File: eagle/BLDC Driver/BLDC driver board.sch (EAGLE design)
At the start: 25 parts, among them J1 SCREWTERM02, Q1 MOSFET-NCHANNEL, Q2 MOSFET-NCHANNEL, Q3 MOSFET-NCHANNEL, Q4 MOSFET-NCHANNEL, Q5 MOSFET-NCHANNEL, Q6 MOSFET-NCHANNEL, U2 AUIRS2334S

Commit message: Started working on new driver board.
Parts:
- removed D1, D2, D6: (no value), CMPE118lib:DIODEHV
- removed U2: AUIRS2334S, ASL:AUIRS2334S
- added 5V: (no value), jumper:JP1E
- added C5, C6: (no value), ASL:CAP0805
- added R2: (no value), ASL:RESISTOR0805-RES
- added U$2: DRV8302, ASL:DRV8302
- C1: value 470nF -> .1uF; device CMPE118lib:CAP1206 -> ASL:CAP0805
- C2: value 470nF -> 4.7uF; device CMPE118lib:CAP1206 -> ASL:CAP0805
- C3: value 470nF -> .015uF; device CMPE118lib:CAP1206 -> ASL:CAP0805
- C4: value 1uF -> (none); device CMPE118lib:CAP1206 -> ASL:CAP0805
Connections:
- removed net N$11: C3.1, D6.C, U2.VB3
- new net CRRNTSNS1: U$1.RA2
- new net CRRNTSNS2: U$1.RA0
- new net N$1: C3.2, U$2.SS_TR
- new net N$4: C4.1, U$2.BST_A
- new net N$5: C4.2, U$2.SH_A
- new net N$6: C5.1, U$2.BST_B
- new net N$8: C6.1, U$2.BST_C
- new net N$9: C6.2, U$2.SH_C
- new net PGND: Q2.S, Q4.S, Q6.S, U$2.GND
- new net PVDD: C1.1, C2.1, Q1.D, Q3.D, Q5.D, U$2.PVDD1, U$2.PVDD2, U$2.PVDD2(1)
- net +UB: no longer Q1.D, Q3.D, Q5.D
- net -UB: no longer Q2.S, Q4.S, Q6.S
- net GND: now also 5V.1, C1.2, C2.2, C3.1, R2.2; no longer C4.2, U2.COM
- net HO1: no longer U2.HO1
- net HO2: no longer U2.HO2
- net HO3: no longer U2.HO3
- net LO1: no longer U2.LO1
- net LO2: no longer U2.LO2
- net LO3: no longer U2.LO3
- net N$3: now also R2.1, U$2.BIAS; no longer C1.1, D1.C, U2.VB1
- net N$7: now also C5.2, U$2.SH_B; no longer C2.1, D2.C, U2.VB2
- net OUTPUTA: no longer C1.2, U2.VS1
- net OUTPUTB: no longer C2.2, U2.VS2
- net OUTPUTC: no longer C3.2, U2.VS3
- net PWM1: now also U$2.INH_A; no longer U2.HIN1, U2.LIN1
- net PWM2: now also U$2.INH_B; no longer U2.HIN2, U2.LIN2
- net PWM3: now also U$2.INH_C; no longer U2.HIN3, U2.LIN3
- net VCC: now also 5V.2; no longer C4.1, D1.A, D2.A, D6.A, U2.VCC
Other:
- moved on the sheet: C1, C2, C3, C4

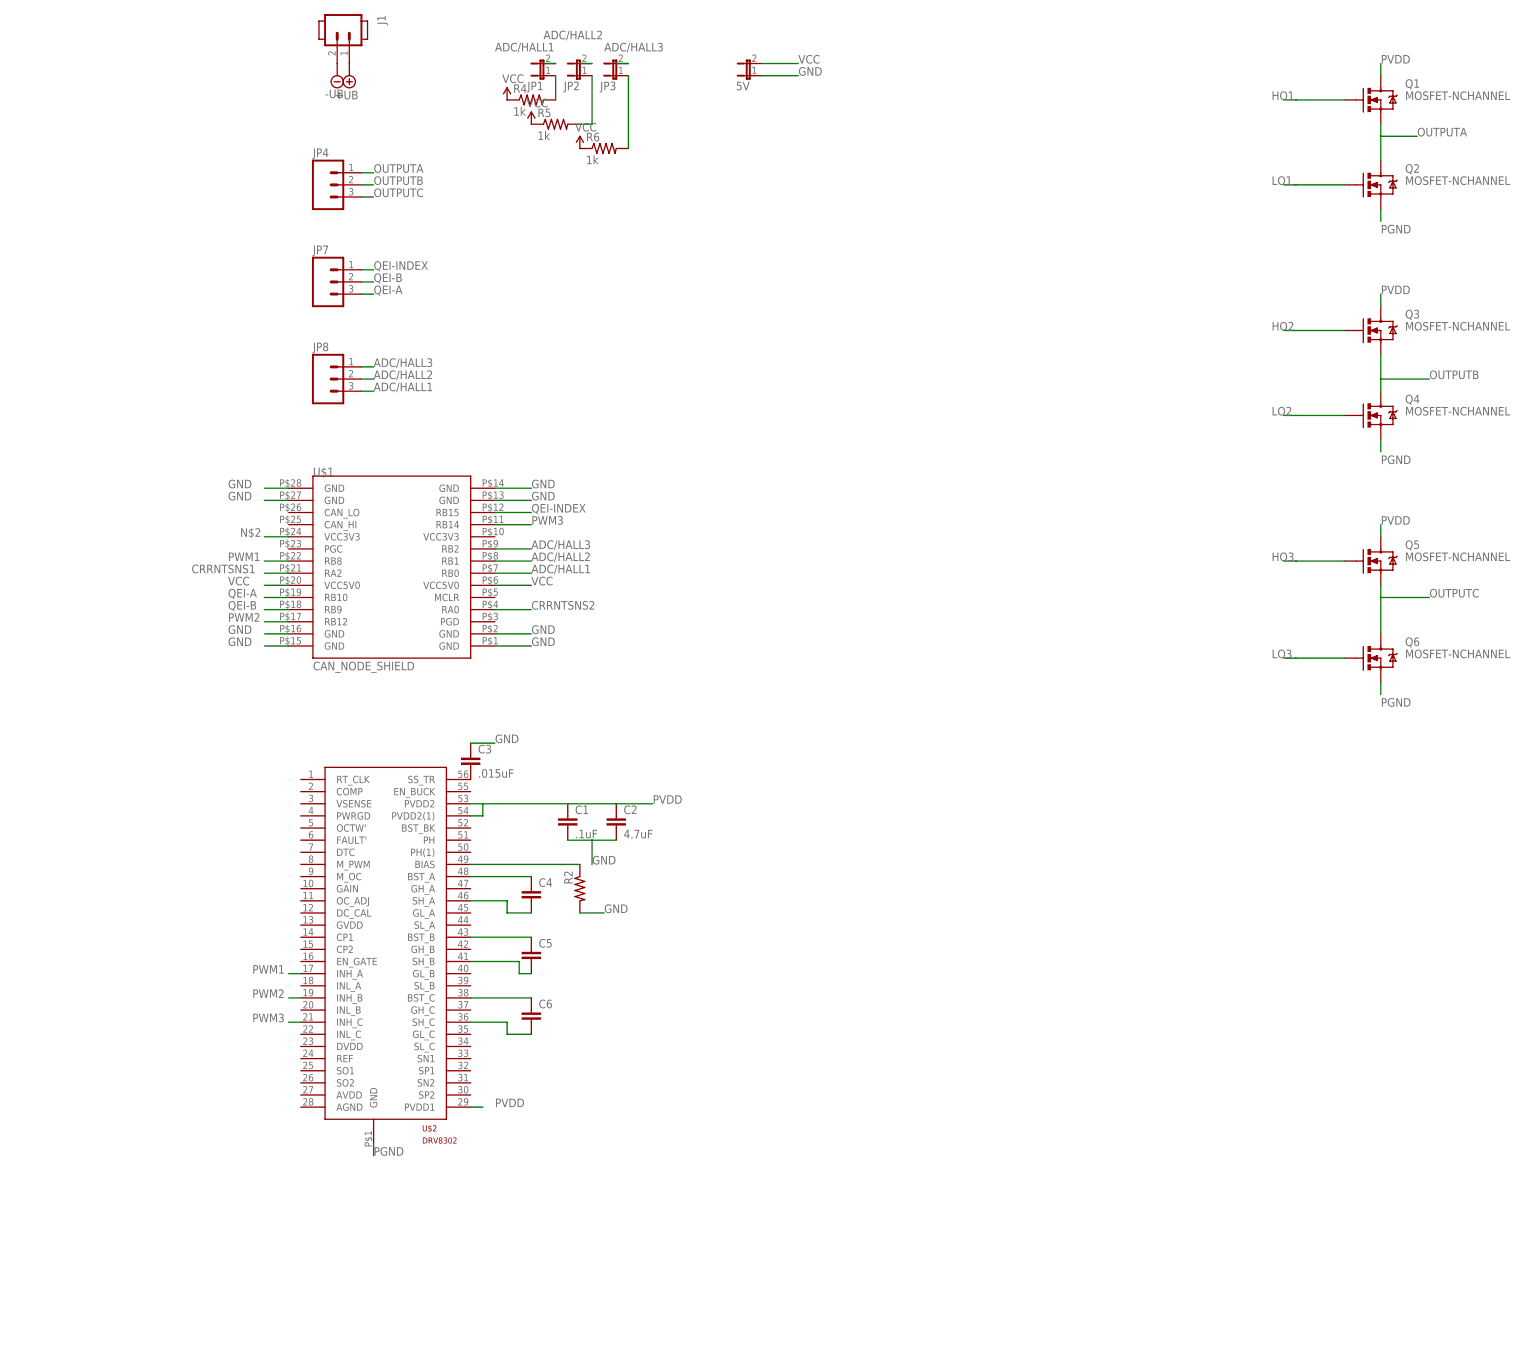
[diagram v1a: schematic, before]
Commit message: Finished BLDC Driver v2.1
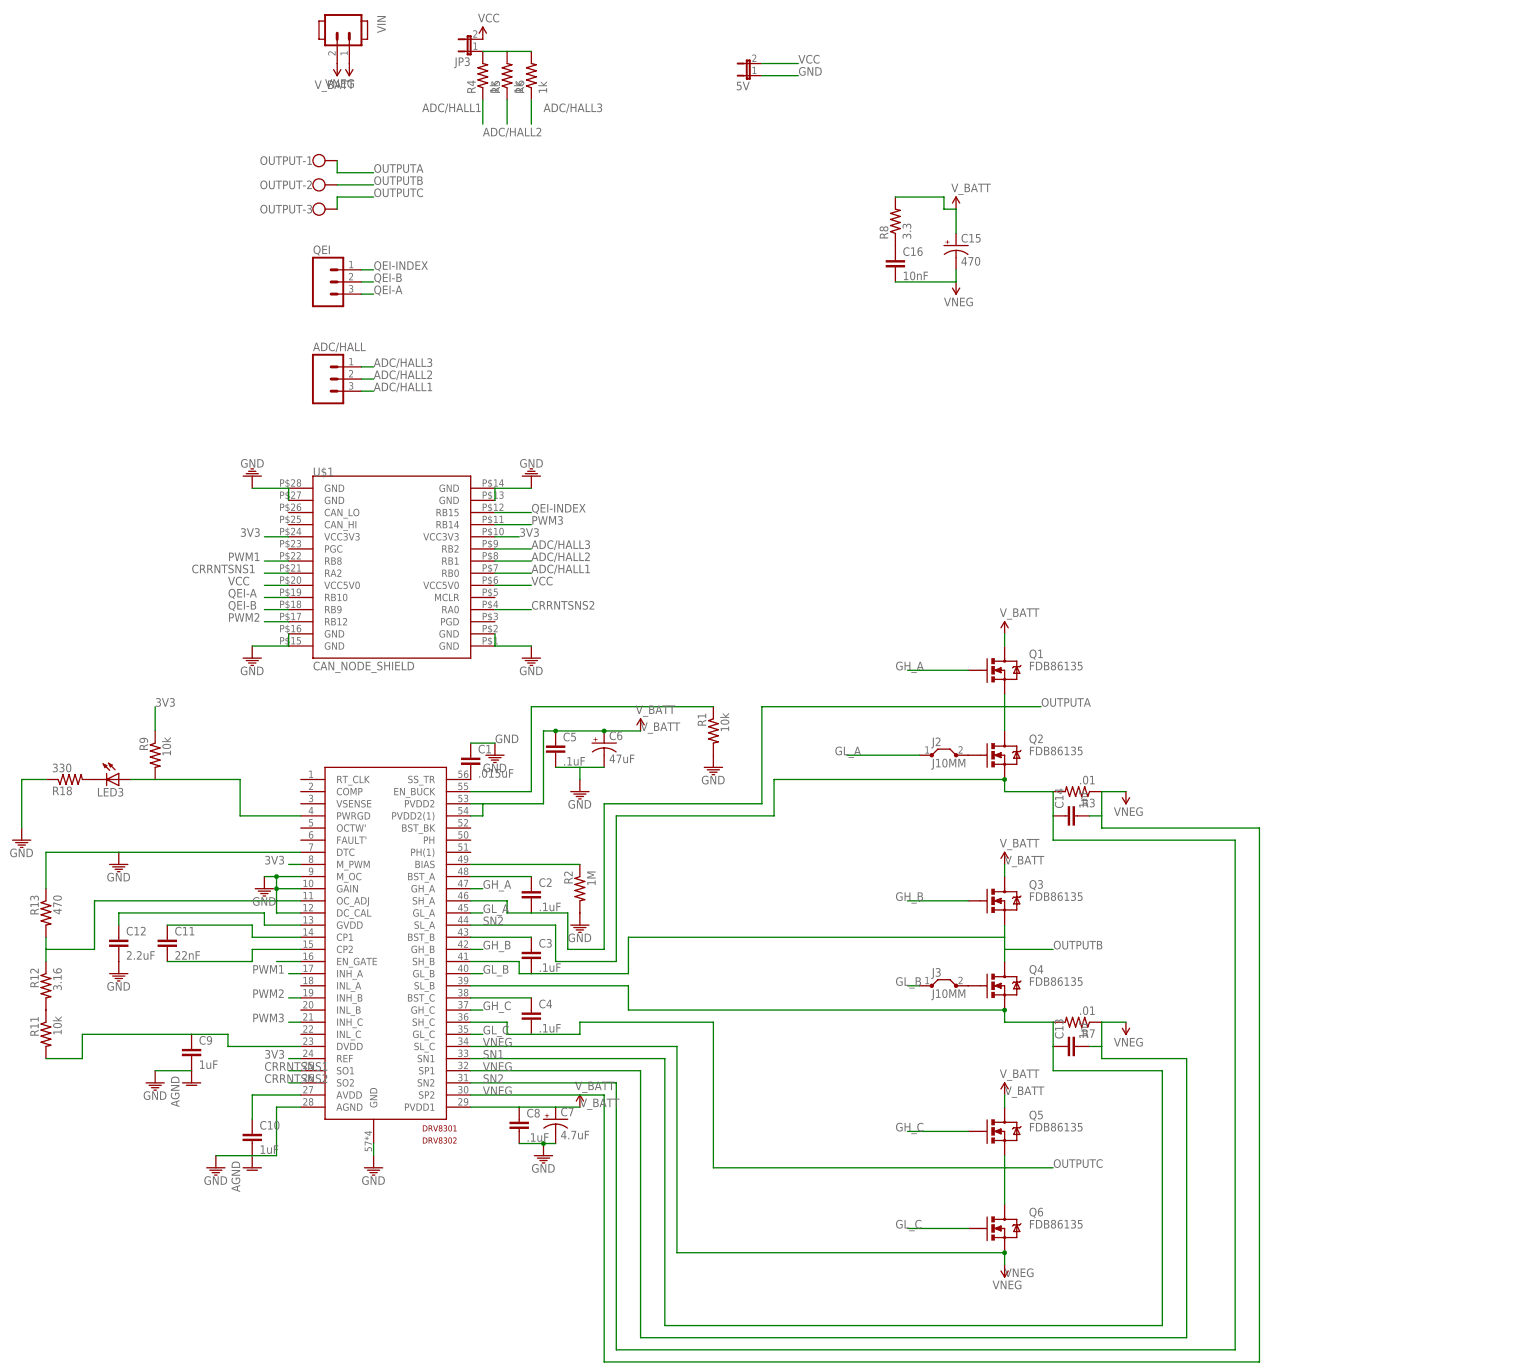
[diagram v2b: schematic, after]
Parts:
- removed JP1, JP2: (no value), jumper:JP1E
- removed JP4: (no value), CMPE118lib:M03SCREW_LOCK
- added C10, C9: 1uF, ASL:CAP1206
- added C11: 22nF, ASL:CAP1206
- added C12: 2.2uF, ASL:CAP1206
- added C13, C14: 1nF, ASL:CAP1206
- added C15: 470, ASL:CAP_POLPTH3
- added C16: 10nF, ASL:CAP1206
- added C7: 4.7uF, ASL:CAP_POLE
- added C8: .1uF, ASL:CAP1206
- added J2, J3: J10MM, jumper:J10MM
- added LED3: (no value), ASL:LED1206
- added OUTPUT: (no value), con-wago-500:W237-103
- added R1, R11, R9: 10k, ASL:RESISTOR0805-RES
- added R12: 3.16, ASL:RESISTOR0805-RES
- added R13: 470, ASL:RESISTOR0805-RES
- added R18: 330, ASL:RESISTOR0805-RES
- added R3, R7: .01, ASL:RESISTOR
- added R8: 3.3, CMPE118lib:RESISTOR1206
- C1: value .1uF -> .015uF; device ASL:CAP0805 -> ASL:CAP1206
- C2: value 4.7uF -> .1uF; device ASL:CAP0805 -> ASL:CAP1206
- C3: value .015uF -> .1uF; device ASL:CAP0805 -> ASL:CAP1206
- C4, C5: value (none) -> .1uF; device ASL:CAP0805 -> ASL:CAP1206
- C6: value (none) -> 47uF; device ASL:CAP0805 -> ASL:CAP_POLE
- Q1, Q2, Q3, Q4, Q5, Q6: value MOSFET-NCHANNEL -> FDB86135
- R2: value (none) -> 1M
- renumbered J1 to VIN, JP7 to QEI, JP8 to ADC/HALL, U$2 to DRV8301
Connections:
- removed net +UB: VIN.1
- removed net -UB: VIN.2
- removed net HO1: Q1.G
- removed net HO2: Q3.G
- removed net HO3: Q5.G
- removed net LO1: Q2.G
- removed net LO2: Q4.G
- removed net LO3: Q6.G
- removed net N$26: JP1.1, R4.2
- removed net N$27: JP2.1, R5.2
- removed net N$28: JP3.1, R6.2
- removed net PGND: DRV8301.GND, Q2.S, Q4.S, Q6.S
- removed net PVDD: C1.1, C2.1, DRV8301.PVDD1, DRV8301.PVDD2, DRV8301.PVDD2(1), Q1.D, Q3.D, Q5.D
- new net 3V3: DRV8301.EN_GATE, DRV8301.M_PWM, DRV8301.REF, R9.1, U$1.VCC3V3@10, U$1.VCC3V3@24
- new net GH_A: DRV8301.GH_A, Q1.G
- new net GH_B: DRV8301.GH_B, Q3.G
- new net GH_C: DRV8301.GH_C, Q5.G
- new net GL_A: DRV8301.GL_A, J2.1
- new net GL_B: DRV8301.GL_B, J3.1
- new net GL_C: DRV8301.GL_C, Q6.G
- new net N$10: DRV8301.EN_BUCK, R1.1
- new net N$11: DRV8301.PWRGD, LED3.A, R9.2
- new net N$12: DRV8301.OC_ADJ, R12.1, R13.2
- new net N$13: JP3.1, R4.2, R5.2, R6.2
- new net N$15: LED3.C, R18.2
- new net N$16: C10.1, DRV8301.AVDD
- new net N$18: C9.1, DRV8301.DVDD, R11.2
- new net N$19: C11.1, DRV8301.CP1
- new net N$20: C11.2, DRV8301.CP2
- new net N$21: C12.1, DRV8301.GVDD
- new net SN1: C13.1, DRV8301.SL_B, DRV8301.SN1, Q4.S, R7.2
- new net SN2: C14.1, DRV8301.SL_A, DRV8301.SN2, Q2.S, R3.2
- new net VNEG: C13.2, C14.2, C15.-, C16.2, DRV8301.SL_C, DRV8301.SP1, DRV8301.SP2, Q6.S, R3.1, R7.1, VIN.2
- new net V_BATT: C15.+, C5.1, C6.+, C7.+, C8.1, DRV8301.PVDD1, DRV8301.PVDD2, DRV8301.PVDD2(1), Q1.D, Q3.D, Q5.D, R8.2, VIN.1
- net ADC/HALL1: now also R6.1; no longer JP1.2
- net ADC/HALL2: now also R5.1; no longer JP2.2
- net ADC/HALL3: now also R4.1; no longer JP3.2
- net CRRNTSNS1: now also DRV8301.SO1
- net CRRNTSNS2: now also DRV8301.SO2
- net GND: now also C1.1, C10.2, C12.2, C5.2, C6.-, C7.-, C8.2, C9.2, DRV8301.AGND, DRV8301.DC_CAL, DRV8301.DTC, DRV8301.GAIN, DRV8301.GND, DRV8301.M_OC, R1.2, R13.1, R18.1; no longer C1.2, C2.2, C3.1
- net N$1: now also C1.2; no longer C3.2
- net N$2: now also J2.2, Q2.G; no longer U$1.VCC3V3@24
- net N$4: now also C2.1; no longer C4.1
- net N$5: now also J3.2, Q4.G; no longer C4.2, DRV8301.SH_A
- net N$6: now also C3.1; no longer C5.1
- net N$7: now also C16.1, R8.1; no longer C5.2, DRV8301.SH_B
- net N$8: now also C4.1; no longer C6.1
- net N$9: now also R11.1, R12.2; no longer C6.2, DRV8301.SH_C
- net OUTPUTA: now also C2.2, DRV8301.SH_A, OUTPUT-1.KL; no longer JP4.1
- net OUTPUTB: now also C3.2, DRV8301.SH_B, OUTPUT-2.KL; no longer JP4.2
- net OUTPUTC: now also C4.2, DRV8301.SH_C, OUTPUT-3.KL; no longer JP4.3
- net VCC: now also JP3.2; no longer R4.1, R5.1, R6.1
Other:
- moved on the sheet: C1, C2, C3, C4, C5, JP3, Q1, Q2, Q3, Q4, Q5, Q6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

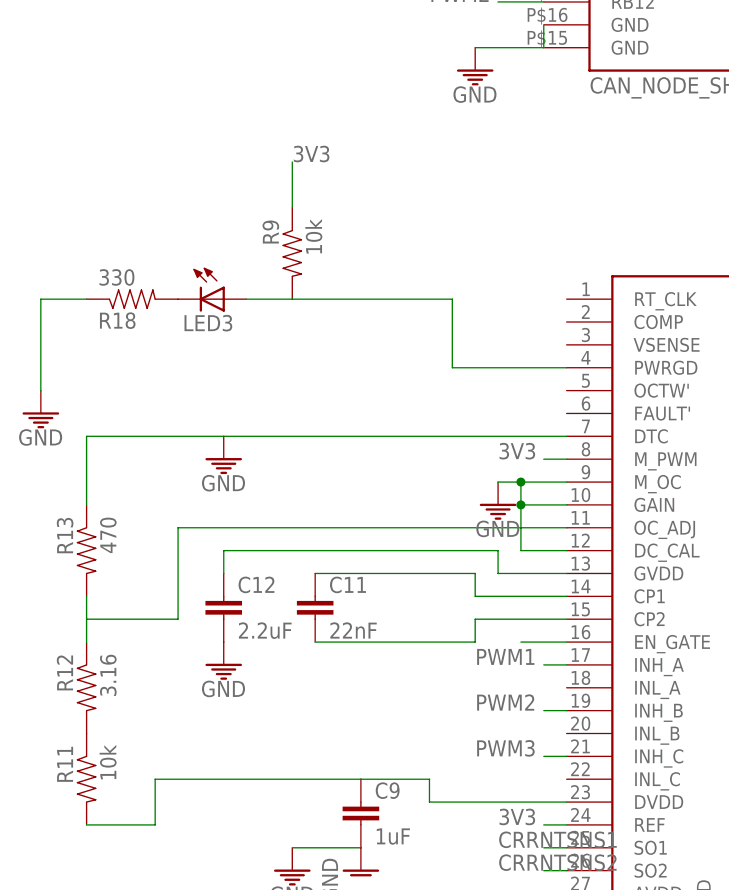
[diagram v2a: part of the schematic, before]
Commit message: Finished v 2 of the BLDC driver board
Finished the alumni board

Finished the MAC.PHY_shield for the ASL CAN node.

Signed-off-by: Pavlo Manovi <pavlo.manovi@gmail.com>
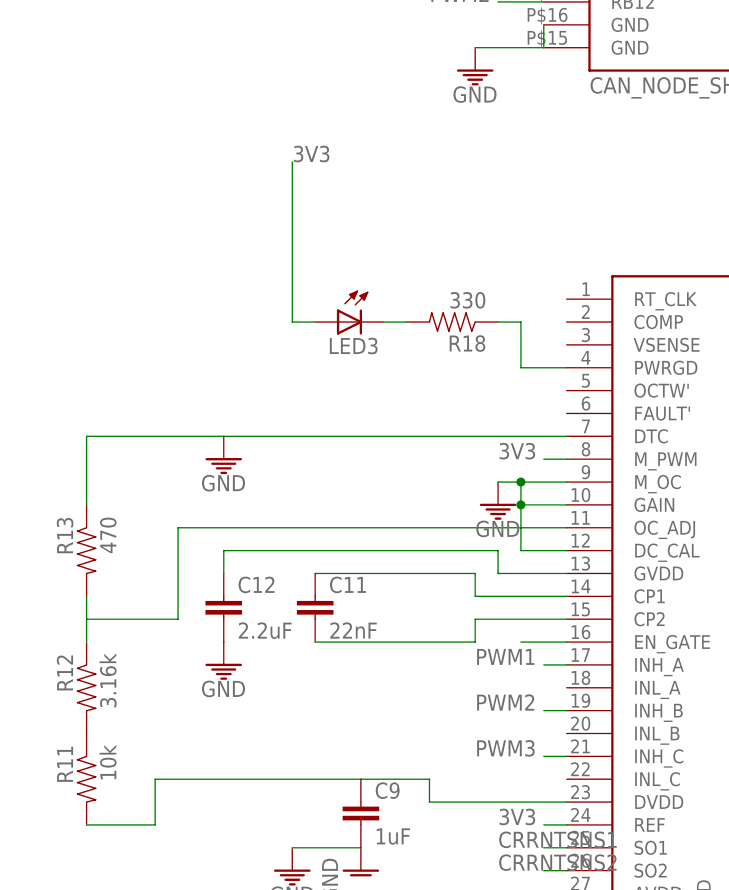
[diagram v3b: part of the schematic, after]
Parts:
- removed R9: 10k, ASL:RESISTOR0805-RES
- R12: value 3.16 -> 3.16k
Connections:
- net 3V3: now also LED3.A; no longer R9.1
- net GND: no longer R18.1
- net N$11: now also R18.1; no longer LED3.A, R9.2
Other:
- moved on the sheet: LED3, R18
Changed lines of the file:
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@@
 <part name="GND15" library="ASL" deviceset="GND" device=""/>
 <part name="R13" library="ASL" deviceset="RESISTOR" device="0805-RES" value="470"/>
-<part name="R12" library="ASL" deviceset="RESISTOR" device="0805-RES" value="3.16"/>
+<part name="R12" library="ASL" deviceset="RESISTOR" device="0805-RES" value="3.16k"/>
 <part name="R11" library="ASL" deviceset="RESISTOR" device="0805-RES" value="10k"/>
-<part name="R9" library="ASL" deviceset="RESISTOR" device="0805-RES" value="10k"/>
 <part name="LED3" library="ASL" deviceset="LED" device="1206"/>
 <part name="R18" library="ASL" deviceset="RESISTOR" device="0805-RES" value="330"/>
-<part name="GND16" library="ASL" deviceset="GND" device=""/>
 </parts>
 <sheets>
@@
 <instance part="R12" gate="G$1" x="-27.94" y="-63.5" rot="MR270"/>
 <instance part="R11" gate="G$1" x="-27.94" y="-73.66" rot="MR270"/>
-<instance part="R9" gate="G$1" x="-5.08" y="-15.24" rot="MR270"/>
-<instance part="LED3" gate="G$1" x="-12.7" y="-20.32" rot="R270"/>
-<instance part="R18" gate="G$1" x="-22.86" y="-20.32" rot="MR180"/>
-<instance part="GND16" gate="1" x="-33.02" y="-33.02"/>
+<instance part="LED3" gate="G$1" x="0" y="-22.86" rot="MR270"/>
+<instance part="R18" gate="G$1" x="12.7" y="-22.86" rot="R180"/>
 </instances>
 <busses>
@@
 <junction x="20.32" y="-40.64"/>
 <junction x="20.32" y="-43.18"/>
-</segment>
-<segment>
-<pinref part="R18" gate="G$1" pin="1"/>
-<pinref part="GND16" gate="1" pin="GND"/>
-<wire x1="-27.94" y1="-20.32" x2="-33.02" y2="-20.32" width="0.2032" layer="91"/>
-<wire x1="-33.02" y1="-20.32" x2="-33.02" y2="-30.48" width="0.2032" layer="91"/>
 </segment>
 </net>
@@
 </segment>
 <segment>
-<wire x1="-5.08" y1="-5.08" x2="-5.08" y2="-10.16" width="0.2032" layer="91"/>
 <label x="-5.08" y="-5.08" size="1.778" layer="95"/>
-<pinref part="R9" gate="G$1" pin="1"/>
+<wire x1="-5.08" y1="-5.08" x2="-5.08" y2="-22.86" width="0.2032" layer="91"/>
+<pinref part="LED3" gate="G$1" pin="A"/>
+<wire x1="-5.08" y1="-22.86" x2="-2.54" y2="-22.86" width="0.2032" layer="91"/>
 </segment>
 <segment>
@@
 </segment>
 </net>
-<net name="N$11" class="0">
-<segment>
-<pinref part="LED3" gate="G$1" pin="A"/>
-<pinref part="R9" gate="G$1" pin="2"/>
-<wire x1="-10.16" y1="-20.32" x2="-5.08" y2="-20.32" width="0.2032" layer="91"/>
-<pinref part="DRV8301" gate="U1" pin="PWRGD"/>
-<wire x1="25.4" y1="-27.94" x2="12.7" y2="-27.94" width="0.2032" layer="91"/>
-<wire x1="12.7" y1="-27.94" x2="12.7" y2="-20.32" width="0.2032" layer="91"/>
-<wire x1="12.7" y1="-20.32" x2="-5.08" y2="-20.32" width="0.2032" layer="91"/>
-</segment>
-</net>
 <net name="N$15" class="0">
 <segment>
 <pinref part="LED3" gate="G$1" pin="C"/>
 <pinref part="R18" gate="G$1" pin="2"/>
+<wire x1="5.08" y1="-22.86" x2="7.62" y2="-22.86" width="0.1524" layer="91"/>
 </segment>
 </net>
@@
 </segment>
 </net>
+<net name="N$11" class="0">
+<segment>
+<pinref part="R18" gate="G$1" pin="1"/>
+<wire x1="17.78" y1="-22.86" x2="20.32" y2="-22.86" width="0.2032" layer="91"/>
+<wire x1="20.32" y1="-22.86" x2="20.32" y2="-27.94" width="0.2032" layer="91"/>
+<pinref part="DRV8301" gate="U1" pin="PWRGD"/>
+<wire x1="20.32" y1="-27.94" x2="25.4" y2="-27.94" width="0.2032" layer="91"/>
+</segment>
+</net>
